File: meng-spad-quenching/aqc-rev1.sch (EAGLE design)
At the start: 137 parts, among them IC1 ADCMP582, IC2 NC7SV74K8X, IC3 LT3032-5, IC4 OPA342, IC5 OPA342, IC6 LTC1711, IC7 DS1100LU-20+, IC8 LT3032-15, IC9 NC7WZ16P6X, J1 VIN_LOGIC, M1 BSS806N, Q1 MMBTH81, Q2 MMBTH81, Q3 MMBTH81, Q4 MMBTH81, Q5 MMBTH81, Q6 MMBTH81, T1 MMBTH10, T2 MMBTH10, T3 MMBTH10, T4 MMBTH10, T5 MMBTH10, T6 MMBTH10, T7 MMBTH10, U1 SN65EPT21DGK, U2 TPS78233DDCT, U3 SN65EPT22DGK, X1 CONN_SPAD, X2 CONN_PHOTON_COUNTER, X3 CONN_FORCE_QUENCH, X4 CONN_VREF_ONE_SHOT_EXT, X5 CONN_VREF_DIAMOND_IBIAS_EXT, X6 CONN_VREF_CASCODE_IBIAS_EXT

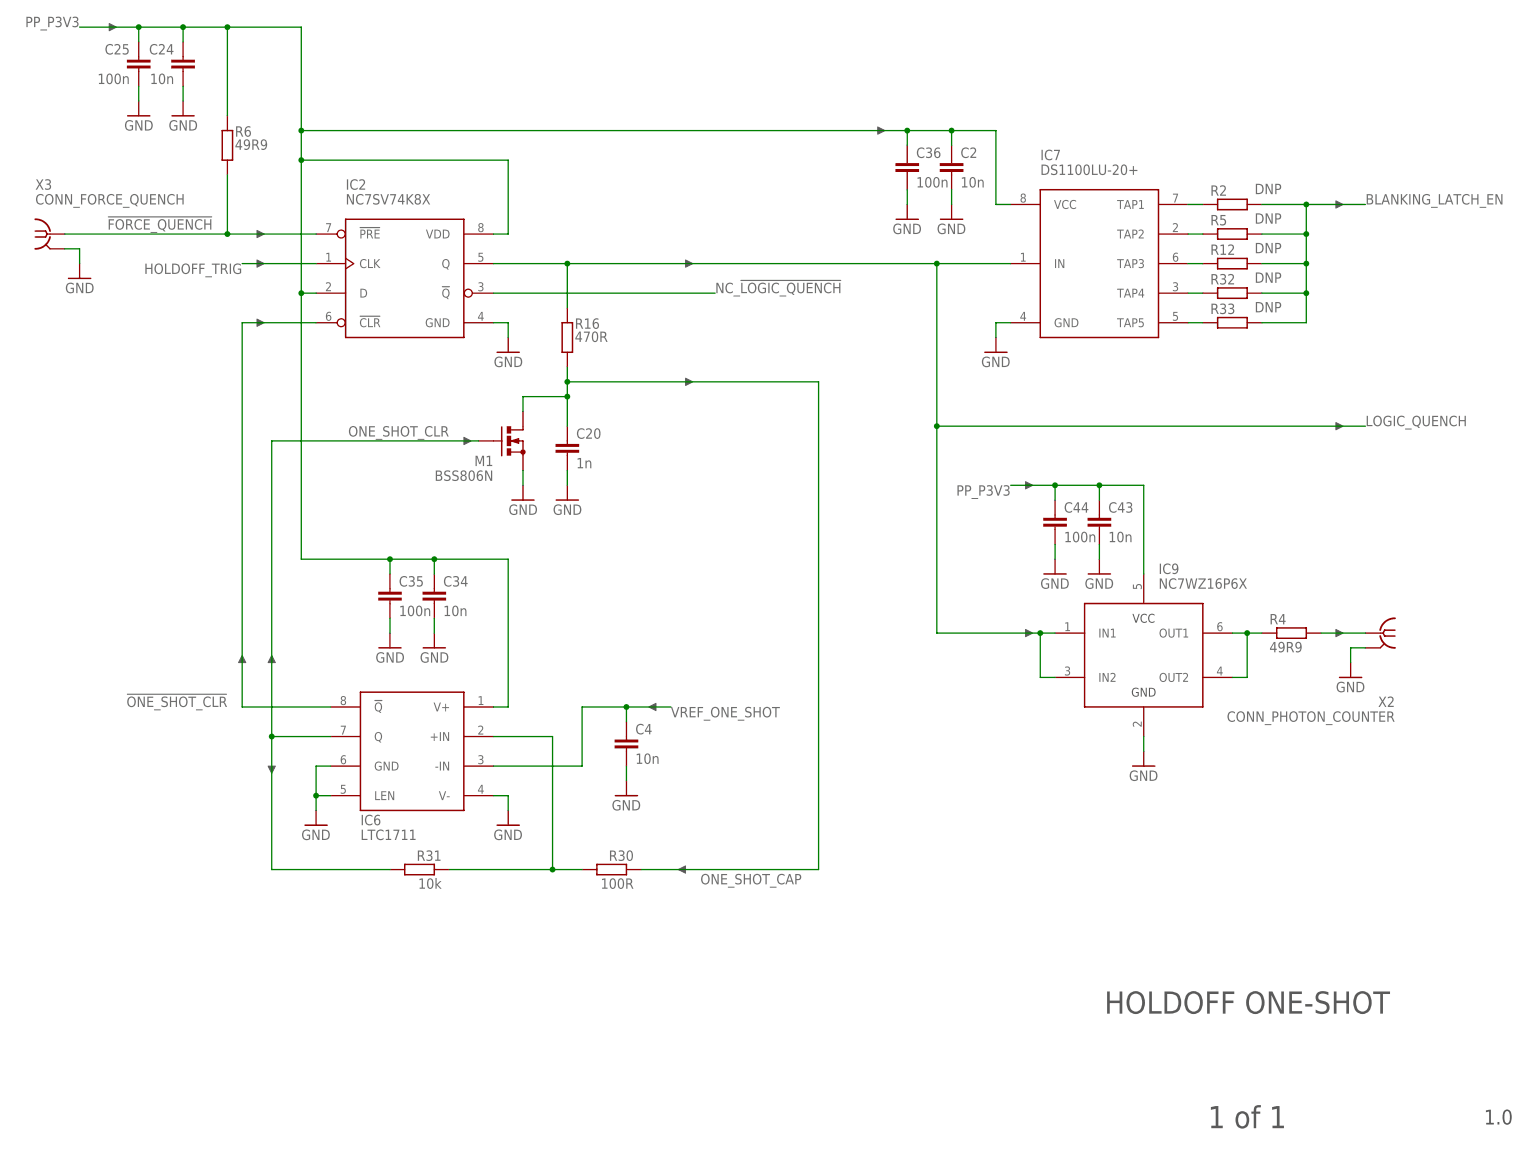
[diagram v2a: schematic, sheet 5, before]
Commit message: More layout, switched delay line to be driven from line driver
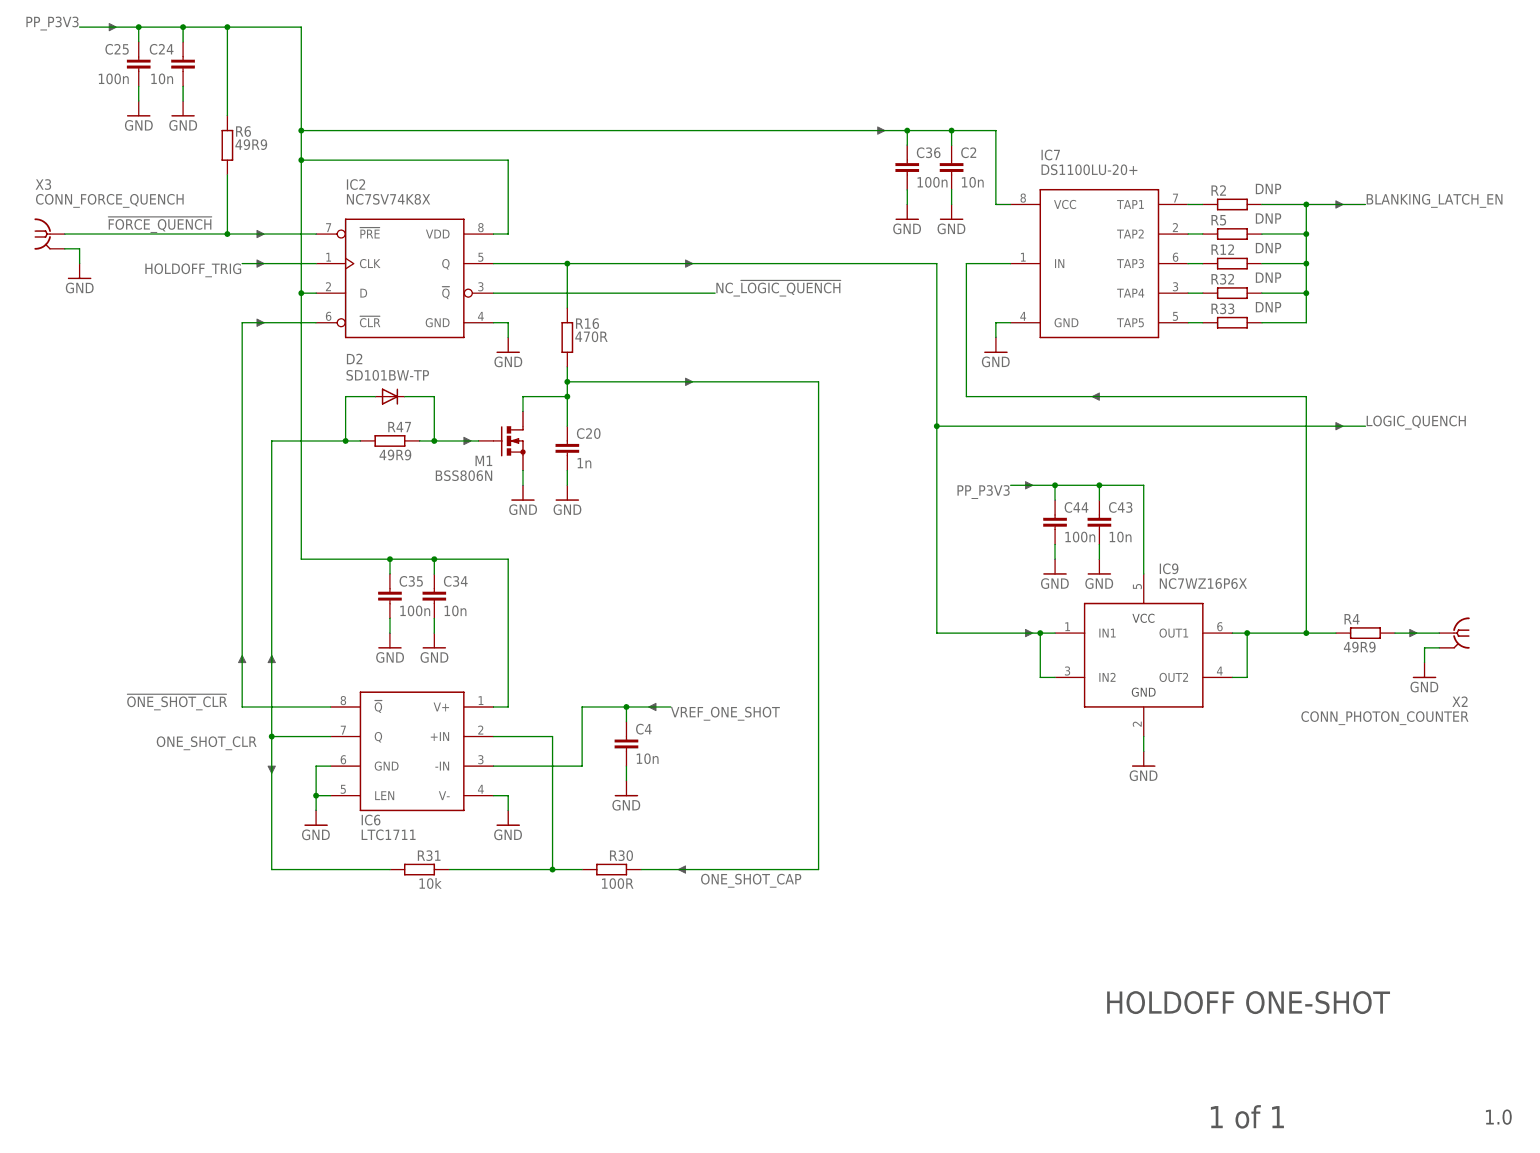
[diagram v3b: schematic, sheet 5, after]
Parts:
- added D2: SD101BW-TP, diode:DIODE-SOD123
- added R47: 49R9, rcl:R-EU_R0603
- C4, C43, C44: device rcl:C-EUC0603 -> rcl:C-EUC0402
- R10, R8, R9: device rcl:R-EU_R0603 -> rcl:R-EU_R0402
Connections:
- new net N$36: D2.C, M1.G, R47.2
- net LOGIC_QUENCH: no longer IC7.IN
- net N$37: now also IC7.IN
- net ONE_SHOT_CLR: now also D2.A, R47.1; no longer M1.G
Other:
- note added: "Max. unterminated length for t_rise = 1ns is ~1in."
- note added: "Reduce loading of d-flop as much as possible"
- moved on the sheet: R4, X2
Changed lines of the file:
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@@
 <part name="DNP18" library="meng" deviceset="ARROW_1DIR" device=""/>
 <part name="DNP19" library="meng" deviceset="ARROW_1DIR" device=""/>
-<part name="R8" library="rcl" deviceset="R-EU_" device="R0603" value="100R"/>
-<part name="R9" library="rcl" deviceset="R-EU_" device="R0603" value="150R"/>
-<part name="R10" library="rcl" deviceset="R-EU_" device="R0603" value="150R"/>
+<part name="R8" library="rcl" deviceset="R-EU_" device="R0402" value="100R"/>
+<part name="R9" library="rcl" deviceset="R-EU_" device="R0402" value="150R"/>
+<part name="R10" library="rcl" deviceset="R-EU_" device="R0402" value="150R"/>
 <part name="GND20" library="supply1" deviceset="GND" device=""/>
 <part name="GND21" library="supply1" deviceset="GND" device=""/>
@@
 <part name="GND13" library="supply1" deviceset="GND" device=""/>
 <part name="DNP41" library="meng" deviceset="ARROW_1DIR" device=""/>
-<part name="C4" library="rcl" deviceset="C-EU" device="C0603" value="10n"/>
+<part name="C4" library="rcl" deviceset="C-EU" device="C0402" value="10n"/>
 <part name="GND14" library="supply1" deviceset="GND" device=""/>
 <part name="R35" library="rcl" deviceset="R-EU_" device="R0603" value="DNP"/>
@@
 <part name="C5" library="rcl" deviceset="C-EU" device="C0603" value="10n"/>
 <part name="IC9" library="meng" deviceset="NC7WZ16P6X" device=""/>
-<part name="C43" library="rcl" deviceset="C-EU" device="C0603" value="10n"/>
-<part name="C44" library="rcl" deviceset="C-EU" device="C0603" value="100n"/>
+<part name="C43" library="rcl" deviceset="C-EU" device="C0402" value="10n"/>
+<part name="C44" library="rcl" deviceset="C-EU" device="C0402" value="100n"/>
 <part name="R4" library="rcl" deviceset="R-EU_" device="R0603" value="49R9"/>
 <part name="GND6" library="supply1" deviceset="GND" device=""/>
@@
 </part>
 <part name="GND79" library="supply1" deviceset="GND" device=""/>
+<part name="R47" library="rcl" deviceset="R-EU_" device="R0603" value="49R9"/>
+<part name="D2" library="diode" deviceset="DIODE-" device="SOD123" value="SD101BW-TP"/>
+<part name="DNP68" library="meng" deviceset="ARROW_1DIR" device=""/>
 </parts>
 <sheets>
@@
 <text x="114.3" y="111.76" size="3.81" layer="97" font="vector" align="center-left">HOLDOFF ONE-SHOT</text>
 <text x="114.3" y="101.6" size="3.81" layer="97" font="vector" align="center-left">CONTROL INPUT CONNECTORS</text>
-<text x="10.16" y="25.4" size="3.81" layer="97">Routing Notes:</text>
+<text x="10.16" y="30.48" size="3.81" layer="97">Routing Notes:</text>
+<text x="10.16" y="22.86" size="2.54" layer="97">Max. unterminated length for t_rise = 1ns is ~1in.</text>
 </plain>
 <instances>
@@
 <text x="266.7" y="8.255" size="2.54" layer="97" font="vector" align="center">1.0</text>
 <text x="223.52" y="8.255" size="3.81" layer="97" font="vector" align="center">1 of 1</text>
-<text x="248.92" y="99.06" size="1.778" layer="98" rot="R180">To pulse counter</text>
+<text x="261.62" y="99.06" size="1.778" layer="98" rot="R180">To pulse counter</text>
 <text x="10.16" y="144.78" size="1.778" layer="98">From control logic</text>
 <text x="10.16" y="142.24" size="1.778" layer="98">Assert before probe has landed</text>
+<text x="187.96" y="134.62" size="1.778" layer="98">Reduce loading of d-flop as much as possible</text>
 </plain>
 <instances>
@@
 <attribute name="VALUE" x="114.3" y="60.96" size="1.778" layer="96"/>
 </instance>
-<instance part="X2" gate="G1" x="246.38" y="91.44" smashed="yes" rot="MR0">
-<attribute name="VALUE" x="248.92" y="76.2" size="1.778" layer="96" rot="MR0"/>
-<attribute name="NAME" x="248.92" y="78.74" size="1.778" layer="95" rot="MR0"/>
-</instance>
-<instance part="GND10" gate="1" x="241.3" y="83.82" smashed="yes">
-<attribute name="VALUE" x="238.76" y="81.28" size="1.778" layer="96"/>
-</instance>
-<instance part="DNP13" gate="G$1" x="238.76" y="91.44" smashed="yes"/>
+<instance part="X2" gate="G1" x="259.08" y="91.44" smashed="yes" rot="MR0">
+<attribute name="VALUE" x="261.62" y="76.2" size="1.778" layer="96" rot="MR0"/>
+<attribute name="NAME" x="261.62" y="78.74" size="1.778" layer="95" rot="MR0"/>
+</instance>
+<instance part="GND10" gate="1" x="254" y="83.82" smashed="yes">
+<attribute name="VALUE" x="251.46" y="81.28" size="1.778" layer="96"/>
+</instance>
+<instance part="DNP13" gate="G$1" x="251.46" y="91.44" smashed="yes"/>
 <instance part="IC9" gate="G$1" x="195.58" y="78.74"/>
 <instance part="C43" gate="G$1" x="198.12" y="111.76" smashed="yes">
@@
 <attribute name="VALUE" x="192.024" y="107.061" size="1.778" layer="96"/>
 </instance>
-<instance part="R4" gate="G$1" x="231.14" y="91.44" smashed="yes" rot="R180">
-<attribute name="NAME" x="227.33" y="92.9386" size="1.778" layer="95"/>
-<attribute name="VALUE" x="227.33" y="88.138" size="1.778" layer="96"/>
+<instance part="R4" gate="G$1" x="243.84" y="91.44" smashed="yes" rot="R180">
+<attribute name="NAME" x="240.03" y="92.9386" size="1.778" layer="95"/>
+<attribute name="VALUE" x="240.03" y="88.138" size="1.778" layer="96"/>
 </instance>
 <instance part="GND6" gate="1" x="205.74" y="68.58" smashed="yes">
@@
 <attribute name="VALUE" x="25.4" y="149.86" size="1.778" layer="96" rot="MR0"/>
 </instance>
+<instance part="R47" gate="G$1" x="76.2" y="124.46" smashed="yes" rot="MR180">
+<attribute name="NAME" x="80.01" y="125.9586" size="1.778" layer="95" rot="MR0"/>
+<attribute name="VALUE" x="80.01" y="121.158" size="1.778" layer="96" rot="MR0"/>
+</instance>
+<instance part="D2" gate="G$1" x="76.2" y="132.08" smashed="yes">
+<attribute name="NAME" x="68.58" y="137.6426" size="1.778" layer="95"/>
+<attribute name="VALUE" x="68.58" y="134.8486" size="1.778" layer="96"/>
+</instance>
+<instance part="DNP68" gate="G$1" x="198.12" y="132.08" smashed="yes" rot="R180"/>
 </instances>
 <busses>
@@
 <segment>
 <pinref part="GND10" gate="1" pin="GND"/>
-<wire x1="241.3" y1="86.36" x2="241.3" y2="88.9" width="0.1524" layer="91"/>
+<wire x1="254" y1="86.36" x2="254" y2="88.9" width="0.1524" layer="91"/>
 <pinref part="X2" gate="G1" pin="GND"/>
-<wire x1="241.3" y1="88.9" x2="243.84" y2="88.9" width="0.1524" layer="91"/>
+<wire x1="254" y1="88.9" x2="256.54" y2="88.9" width="0.1524" layer="91"/>
 </segment>
 <segment>
@@
 <junction x="106.68" y="154.94"/>
 <label x="243.84" y="127" size="1.778" layer="95"/>
-<pinref part="IC7" gate="G$1" pin="IN"/>
 <wire x1="106.68" y1="154.94" x2="170.18" y2="154.94" width="0.1524" layer="91"/>
-<wire x1="170.18" y1="154.94" x2="182.88" y2="154.94" width="0.1524" layer="91"/>
 <wire x1="170.18" y1="154.94" x2="170.18" y2="127" width="0.1524" layer="91"/>
 <wire x1="170.18" y1="127" x2="243.84" y2="127" width="0.1524" layer="91"/>
-<junction x="170.18" y="154.94"/>
 <pinref part="IC9" gate="G$1" pin="IN2"/>
 <wire x1="190.5" y1="83.82" x2="187.96" y2="83.82" width="0.1524" layer="91"/>
@@
 <net name="ONE_SHOT_CLR" class="0">
 <segment>
-<pinref part="M1" gate="G$1" pin="G"/>
 <pinref part="R31" gate="G$1" pin="1"/>
 <wire x1="76.2" y1="50.8" x2="55.88" y2="50.8" width="0.1524" layer="91"/>
@@
 <wire x1="55.88" y1="73.66" x2="66.04" y2="73.66" width="0.1524" layer="91"/>
 <junction x="55.88" y="73.66"/>
-<wire x1="91.44" y1="124.46" x2="55.88" y2="124.46" width="0.1524" layer="91"/>
 <wire x1="55.88" y1="124.46" x2="55.88" y2="73.66" width="0.1524" layer="91"/>
-<label x="86.36" y="127" size="1.778" layer="95" rot="R180"/>
+<label x="53.34" y="73.66" size="1.778" layer="95" rot="R180"/>
+<pinref part="R47" gate="G$1" pin="1"/>
+<wire x1="55.88" y1="124.46" x2="68.58" y2="124.46" width="0.1524" layer="91"/>
+<pinref part="D2" gate="G$1" pin="A"/>
+<wire x1="68.58" y1="124.46" x2="71.12" y2="124.46" width="0.1524" layer="91"/>
+<wire x1="73.66" y1="132.08" x2="68.58" y2="132.08" width="0.1524" layer="91"/>
+<wire x1="68.58" y1="132.08" x2="68.58" y2="124.46" width="0.1524" layer="91"/>
+<junction x="68.58" y="124.46"/>
 </segment>
 </net>
@@
 <segment>
 <pinref part="X2" gate="G1" pin="1"/>
-<wire x1="236.22" y1="91.44" x2="243.84" y2="91.44" width="0.1524" layer="91"/>
+<wire x1="248.92" y1="91.44" x2="256.54" y2="91.44" width="0.1524" layer="91"/>
 <pinref part="R4" gate="G$1" pin="1"/>
 </segment>
@@
 <wire x1="223.52" y1="83.82" x2="223.52" y2="91.44" width="0.1524" layer="91"/>
 <pinref part="R4" gate="G$1" pin="2"/>
-<wire x1="223.52" y1="91.44" x2="226.06" y2="91.44" width="0.1524" layer="91"/>
+<wire x1="223.52" y1="91.44" x2="233.68" y2="91.44" width="0.1524" layer="91"/>
 <junction x="223.52" y="91.44"/>
+<wire x1="233.68" y1="91.44" x2="238.76" y2="91.44" width="0.1524" layer="91"/>
+<wire x1="233.68" y1="91.44" x2="233.68" y2="132.08" width="0.1524" layer="91"/>
+<wire x1="233.68" y1="132.08" x2="175.26" y2="132.08" width="0.1524" layer="91"/>
+<wire x1="175.26" y1="132.08" x2="175.26" y2="154.94" width="0.1524" layer="91"/>
+<pinref part="IC7" gate="G$1" pin="IN"/>
+<wire x1="175.26" y1="154.94" x2="182.88" y2="154.94" width="0.1524" layer="91"/>
+<junction x="233.68" y="91.44"/>
 </segment>
 </net>
@@
 </segment>
 </net>
+<net name="N$36" class="0">
+<segment>
+<pinref part="R47" gate="G$1" pin="2"/>
+<pinref part="M1" gate="G$1" pin="G"/>
+<wire x1="81.28" y1="124.46" x2="83.82" y2="124.46" width="0.1524" layer="91"/>
+<pinref part="D2" gate="G$1" pin="C"/>
+<wire x1="83.82" y1="124.46" x2="91.44" y2="124.46" width="0.1524" layer="91"/>
+<wire x1="78.74" y1="132.08" x2="83.82" y2="132.08" width="0.1524" layer="91"/>
+<wire x1="83.82" y1="132.08" x2="83.82" y2="124.46" width="0.1524" layer="91"/>
+<junction x="83.82" y="124.46"/>
+</segment>
+</net>

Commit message: More routing. 10 airwires!
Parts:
- added C45, C46: 10n, rcl:C-EUC0402
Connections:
- net GND: now also C45.2, C46.2
- net VREF_CASCODE_IBIAS: now also C45.1
- net VREF_DIAMOND_IBIAS: now also C46.1
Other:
- moved on the sheet: C29, C30, IC5, R27, R29, T7
